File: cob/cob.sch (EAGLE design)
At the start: 36 parts

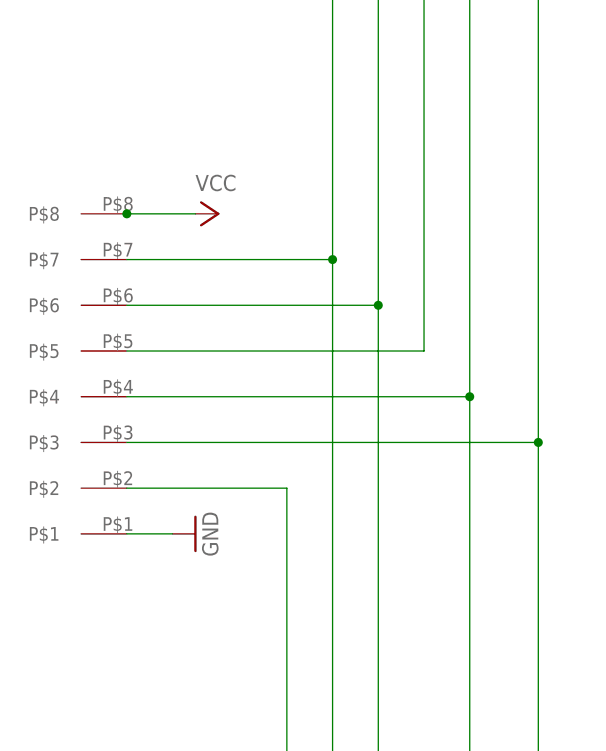
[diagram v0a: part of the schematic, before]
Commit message: fixed connections to cob board
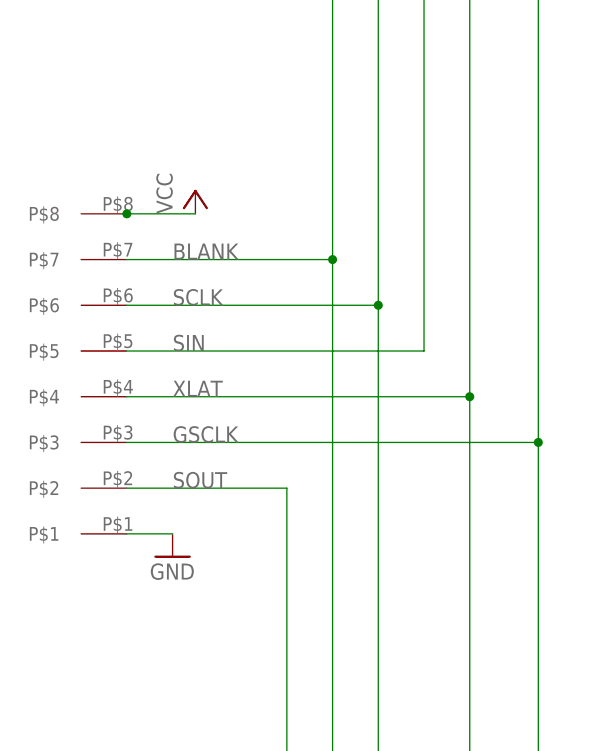
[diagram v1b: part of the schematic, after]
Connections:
- net N$34 renamed XLAT
- net N$35 renamed GSCLK
- net N$37 renamed SOUT
- net N$6 renamed BLANK
- net N$7 renamed SCLK
- net N$8 renamed SIN
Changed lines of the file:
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@@
 <instance part="R3" gate="G$1" x="170.18" y="-116.84" rot="R180"/>
 <instance part="R4" gate="G$1" x="170.18" y="30.48" rot="R180"/>
-<instance part="GND16" gate="1" x="101.6" y="-43.18" rot="R90"/>
+<instance part="GND16" gate="1" x="99.06" y="-45.72"/>
 <instance part="U$1" gate="G$1" x="185.42" y="12.7"/>
 <instance part="U$2" gate="G$1" x="185.42" y="-134.62"/>
@@
 <instance part="P+2" gate="VCC" x="170.18" y="-99.06" rot="R90"/>
 <instance part="P+3" gate="VCC" x="170.18" y="-73.66" rot="R90"/>
-<instance part="P+5" gate="VCC" x="104.14" y="-7.62" rot="R270"/>
+<instance part="P+5" gate="VCC" x="101.6" y="-5.08"/>
 <instance part="GND1" gate="1" x="160.02" y="-132.08"/>
 <instance part="U$3" gate="G$1" x="93.98" y="-43.18" rot="R90"/>
@@
 </segment>
 </net>
-<net name="N$6" class="0">
+<net name="BLANK" class="0">
 <segment>
 <pinref part="U$1" gate="G$1" pin="BLANK"/>
@@
 <wire x1="116.84" y1="-12.7" x2="93.98" y2="-12.7" width="0.1524" layer="91"/>
 <junction x="116.84" y="-12.7"/>
-</segment>
-</net>
-<net name="N$7" class="0">
+<label x="99.06" y="-12.7" size="1.778" layer="95"/>
+</segment>
+</net>
+<net name="SCLK" class="0">
 <segment>
 <pinref part="U$1" gate="G$1" pin="SCLK"/>
@@
 <junction x="121.92" y="-17.78"/>
 <pinref part="U$3" gate="G$1" pin="P$6"/>
-</segment>
-</net>
-<net name="N$8" class="0">
+<label x="99.06" y="-17.78" size="1.778" layer="95"/>
+</segment>
+</net>
+<net name="SIN" class="0">
 <segment>
 <pinref part="U$1" gate="G$1" pin="SIN"/>
@@
 <wire x1="127" y1="-22.86" x2="93.98" y2="-22.86" width="0.1524" layer="91"/>
 <pinref part="U$3" gate="G$1" pin="P$5"/>
+<label x="99.06" y="-22.86" size="1.778" layer="95"/>
 </segment>
 </net>
@@
 </segment>
 </net>
-<net name="N$34" class="0">
+<net name="XLAT" class="0">
 <segment>
 <pinref part="U$1" gate="G$1" pin="XLAT"/>
@@
 <junction x="132.08" y="-27.94"/>
 <pinref part="U$3" gate="G$1" pin="P$4"/>
-</segment>
-</net>
-<net name="N$35" class="0">
+<label x="99.06" y="-27.94" size="1.778" layer="95"/>
+</segment>
+</net>
+<net name="GSCLK" class="0">
 <segment>
 <pinref part="U$1" gate="G$1" pin="GSCLK"/>
@@
 <junction x="139.7" y="-33.02"/>
 <pinref part="U$3" gate="G$1" pin="P$3"/>
-</segment>
-</net>
-<net name="N$37" class="0">
+<label x="99.06" y="-33.02" size="1.778" layer="95"/>
+</segment>
+</net>
+<net name="SOUT" class="0">
 <segment>
 <pinref part="U$2" gate="G$1" pin="SOUT"/>
@@
 <wire x1="111.76" y1="-38.1" x2="93.98" y2="-38.1" width="0.1524" layer="91"/>
 <pinref part="U$3" gate="G$1" pin="P$2"/>
-</segment>
-</net>
+<label x="99.06" y="-38.1" size="1.778" layer="95"/>
+</segment>
+</net>
